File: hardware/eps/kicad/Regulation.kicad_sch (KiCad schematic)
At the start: 28 parts, among them U2 TPS62933FDRLR, U3 TPS62933FDRLR

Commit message: attempt to convert altium to kicad, lost foot prints, not good
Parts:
- renumbered C12 to C16, C13 to C25, C14 to C26, C15 to C27, C8 to C28, C40 to C33, C10 to C34, C11 to C35, C21 to C36, C22 to C37, C23 to C38, C24 to C39, C17 to C41, C18 to C42, C19 to C43, C20 to C44, L2 to L4, L3 to L5, R20 to R18, R11 to R19, R10 to R22, R21 to R23, R12 to R24, R15 to R25, R14 to R26, R13 to R27, U2 to U4, U3 to U5
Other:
- note removed: "${##}"
- note removed: "${#}"
- note removed: "${DRAWNBY}"
- note removed: "${REVISION}"
- note removed: "${TITLE}"
- moved on the sheet: C16, C25, C26, C27, C28, C33, C34, C35, C36, C37, C38, C39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

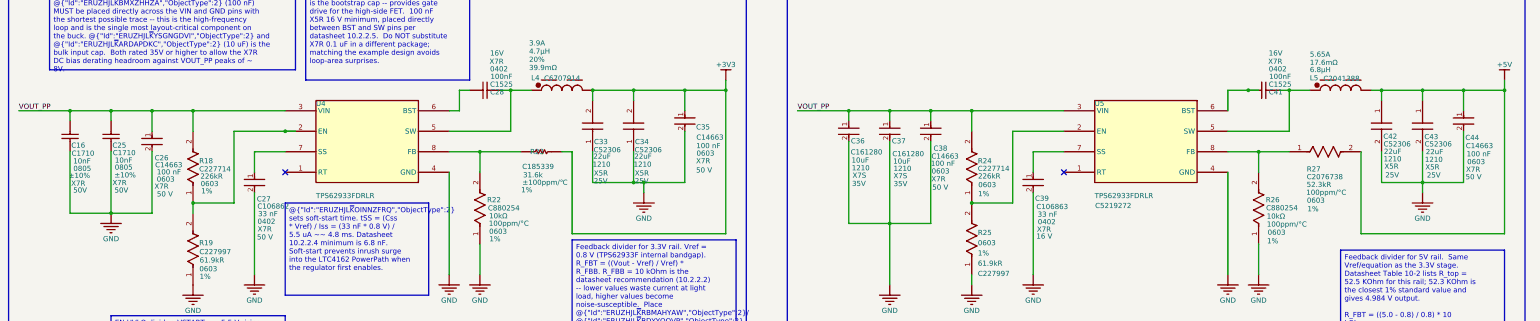
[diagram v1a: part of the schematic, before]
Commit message: eps/kicad: assemble the schematic hierarchy and link it to the PCB
  The three .kicad_sch files were independent roots from the Altium import.
  Opening the project showed only the root's 17 components; the other 60
  were in files KiCad had no path to. Separately, the PCB shared no UUIDs
  at all with any schematic -- it had been imported independently, so the
  board-to-schematic link did not exist rather than being broken.

  Both are now fixed. Root sheet carries sheet symbols for Regulation and
  Solar_Charger, and all 77 footprints link to their symbols: 17 on the
  root, 28 in Regulation, 32 in Solar_Charger, matching the schematics
  exactly. Sheet-local nets picked up hierarchical paths, which cleared
  the "via connected to unknown net" warnings.

  Getting there took several passes and two things had to be repaired
  first.

  Annotation. Building the hierarchy in KiCad re-annotated the child
  sheets -- Solar_Charger went J1-J8 to J11-J18, C1-C24 became C41-C52 --
  because a duplicate J5 blocked the assembly. The refdes are the only
  link to the board, so 69 footprints were deleted as orphans. Every
  symbol UUID survived, so the old annotation was restored exactly by
  UUID, and the board was restored from the previous commit. The J5
  collision is resolved properly: J5 is the JST connector, and the XT30
  that shared its designator is now J10, on both the schematic and the
  board.

  Footprint fields. The import left them unusable -- only 5 of 40 carried
  a library prefix, and 10 pointed at
  C__Users_dng_Documents_AltiumLL_SamacSys.PcbLib, a Windows path from the
  machine that ran the import. All 77 are now the board's own qualified
  ids, which removed about 60 "missing a library name" warnings per
  update.

  The last 11 footprints would not link no matter how the update dialog
  was configured: KiCad matched 66 by UUID path and never fell back to
  reference designators for the remainder. Their paths were written
  directly instead, following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
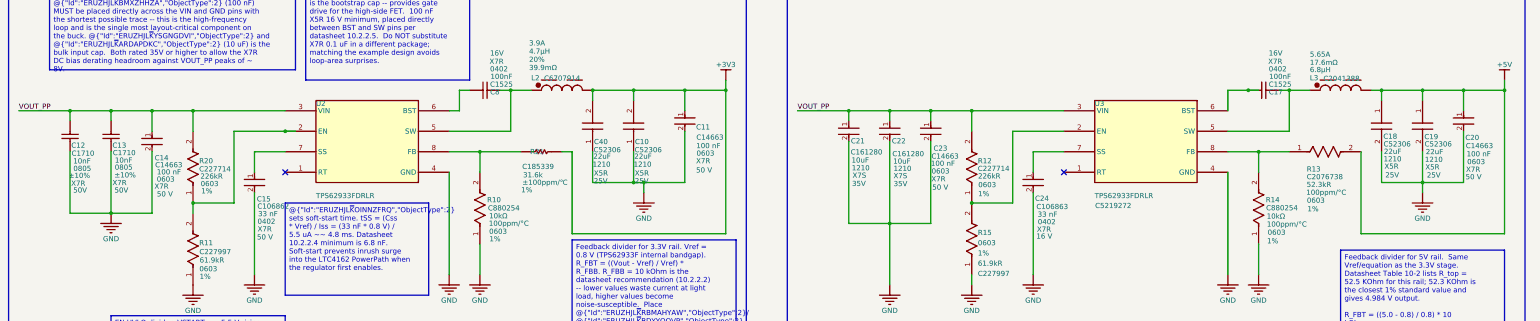
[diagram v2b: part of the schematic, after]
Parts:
- C10: renamed from C34; footprint C__Users_dng_Documents_AltiumLL_SamacSys.PcbLib:CAPC3225X270N -> SamacSys:CAPC3225X270N
- C11: renamed from C35; footprint FP-CC0603-DA-MFG -> Vault:FP-CC0603-DA-MFG
- C12: renamed from C16; footprint CAPC2013X75X45LL10T25 -> Vault:CAPC2013X75X45LL10T25
- C13: renamed from C25; footprint CAPC2013X75X45LL10T25 -> Vault:CAPC2013X75X45LL10T25
- C14: renamed from C26; footprint FP-CC0603-DA-MFG -> Vault:FP-CC0603-DA-MFG
- C15: renamed from C27; footprint FP-CC0402-MFG -> Vault:FP-CC0402-MFG
- C17: renamed from C41; footprint CAPC1050X55X23ML05T13 -> Vault:CAPC1050X55X23ML05T13
- C18: renamed from C42; footprint C__Users_dng_Documents_AltiumLL_SamacSys.PcbLib:CAPC3225X270N -> SamacSys:CAPC3225X270N
- C19: renamed from C43; footprint C__Users_dng_Documents_AltiumLL_SamacSys.PcbLib:CAPC3225X270N -> SamacSys:CAPC3225X270N
- C20: renamed from C44; footprint FP-CC0603-DA-MFG -> Vault:FP-CC0603-DA-MFG
- C21: renamed from C36; footprint FP-GCM32E-0_3-IPC_B -> Vault:FP-GCM32E-0_3-IPC_B
- C22: renamed from C37; footprint FP-GCM32E-0_3-IPC_B -> Vault:FP-GCM32E-0_3-IPC_B
- C23: renamed from C38; footprint FP-CC0603-DA-MFG -> Vault:FP-CC0603-DA-MFG
- C24: renamed from C39; footprint FP-CC0402-MFG -> Vault:FP-CC0402-MFG
- C40: renamed from C33; footprint C__Users_dng_Documents_AltiumLL_SamacSys.PcbLib:CAPC3225X270N -> SamacSys:CAPC3225X270N
- C8: renamed from C28; footprint CAPC1050X55X23ML05T13 -> Vault:CAPC1050X55X23ML05T13
- L2: renamed from L4; footprint WE-MAPI_4030 -> Vault:WE-MAPI_4030
- L3: renamed from L5; footprint WE-XHMI_6060 -> Vault:WE-XHMI_6060
- R10: renamed from R22; footprint FP-SG73P1J-MFG -> Vault:FP-SG73P1J-MFG
- R11: renamed from R19; footprint FP-AC0603-IPC_C -> Vault:FP-AC0603-IPC_C
- R12: renamed from R24; footprint FP-AC0603-IPC_B -> Vault:FP-AC0603-IPC_B
- R13: renamed from R27; footprint FP-CRCW0603-e3-IPC_B -> Vault:FP-CRCW0603-e3-IPC_B
- R14: renamed from R26; footprint FP-SG73P1J-MFG -> Vault:FP-SG73P1J-MFG
- R15: renamed from R25; footprint FP-AC0603-IPC_C -> Vault:FP-AC0603-IPC_C
- R20: renamed from R18; footprint FP-AC0603-IPC_B -> Vault:FP-AC0603-IPC_B
- R21: renamed from R23; footprint RESC1608X55X25NL10T15 -> Vault:RESC1608X55X25NL10T15
- U2: renamed from U4; footprint SOT5X3-8_DRL_TEX -> Vault:SOT5X3-8_DRL_TEX
- U3: renamed from U5; footprint SOT5X3-8_DRL_TEX -> Vault:SOT5X3-8_DRL_TEX
